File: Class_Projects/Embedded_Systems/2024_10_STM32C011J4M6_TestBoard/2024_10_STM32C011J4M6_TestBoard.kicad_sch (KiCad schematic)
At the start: 21 parts, among them J2 SWD_Conn, J3 USB_C_Receptacle_USB2.0_14P, U1 STM32C011J4Mx, U2 FT230XS, U3 LD1117S33TR_SOT223

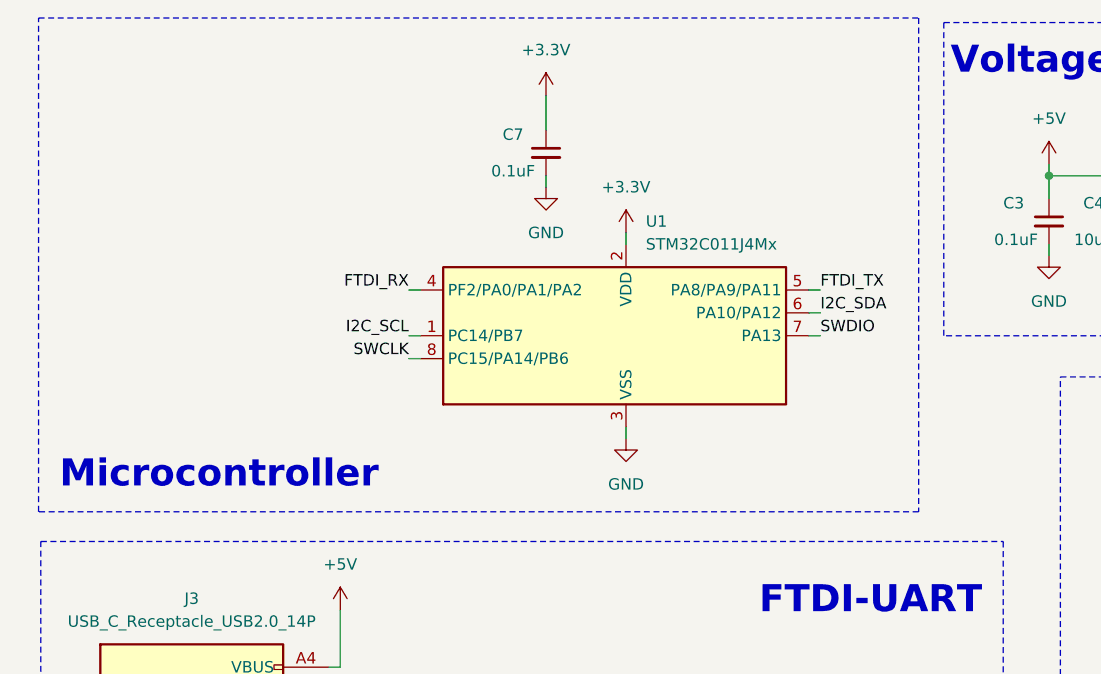
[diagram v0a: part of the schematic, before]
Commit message: I2C resistor addded to the PCB
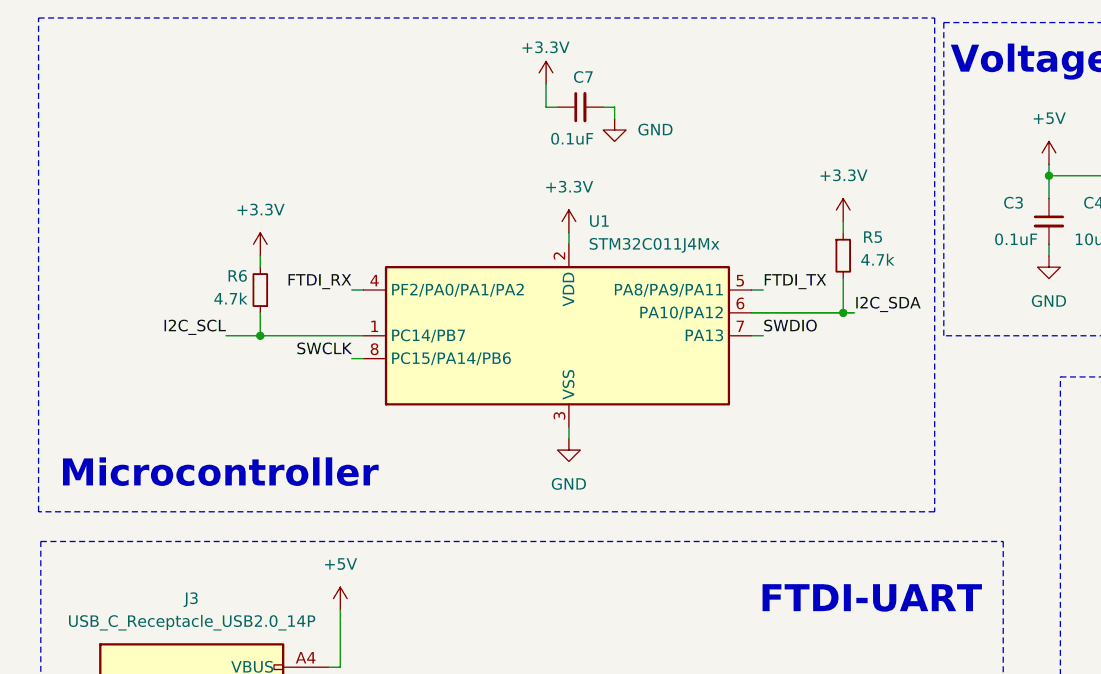
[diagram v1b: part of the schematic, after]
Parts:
- added R5, R6: 4.7k, Resistor_SMD:R_0603_1608Metric_Pad0.98x0.95mm_HandSolder, symbol Device:R_Small
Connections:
- net +3.3V: now also R5.1, R6.2
- net I2C_SCL: now also R6.1
- net I2C_SDA: now also R5.2
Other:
- moved on the sheet: C7, U1
